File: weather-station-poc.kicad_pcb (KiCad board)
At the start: 4 copper layers, 155 x 88 mm, 135 parts, among them IC1 632723100011, IC2 TCPP01-M12, IC3 USBLC6-2SC6, IC4 BME690, IC5 S2-LPQTR, IC6 BALF-SPI2-01D3, IC7 STSAFA110S8OCD03, J1 Conn_ARM_JTAG_SWD_10, J2 61300311121, J3 61300311121, J4 61300511121, J5 61300311121, J6 687140149022, J7 687110183622, Q1 STL11N3LLH6, U1 STM32U5G9ZJTxQ, U2 BME280, U3 BMP581, Y1 NX2016SA-16MHZ-EXS00A-CS07826, Y2 NX2012SA-32.768K-STD-MUB-1, Y3 NX1612SA-50M-EXS00A-CS08403

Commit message: Update weather-station-poc.kicad_pcb
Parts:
- C1, C2, C3, C4, D1, D2, IC2, IC3, Q1, R1, R12, R13, R14, R15, R16, R17, R2, R3, R4: moved to B.Cu
- moved J5 180.7 mm to (158.0, 53.7)
- moved J3 171.5 mm to (148.9, 53.7)
- moved J2 162.4 mm to (139.7, 53.7)
- moved S2 160.4 mm to (72.0, 78.8), turned to -90 degrees
- moved J4 150.3 mm to (125.2, 53.7)
- moved R17 132.0 mm to (97.7, 72.5)
- moved C36 128.3 mm to (236.5, 94.4)
- moved C37 128.3 mm to (236.5, 96.9)
- moved C38 128.3 mm to (236.5, 99.4)
- moved C39 128.3 mm to (236.5, 101.9)
- moved C40 128.3 mm to (236.5, 104.4)
- moved C41 128.3 mm to (236.5, 107.0)
- moved R16 127.6 mm to (97.7, 75.0)
- moved U3 124.5 mm to (221.9, 86.7)
- moved IC4 124.0 mm to (222.0, 81.3)
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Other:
- board size 155 x 88 mm -> 160 x 80 mm

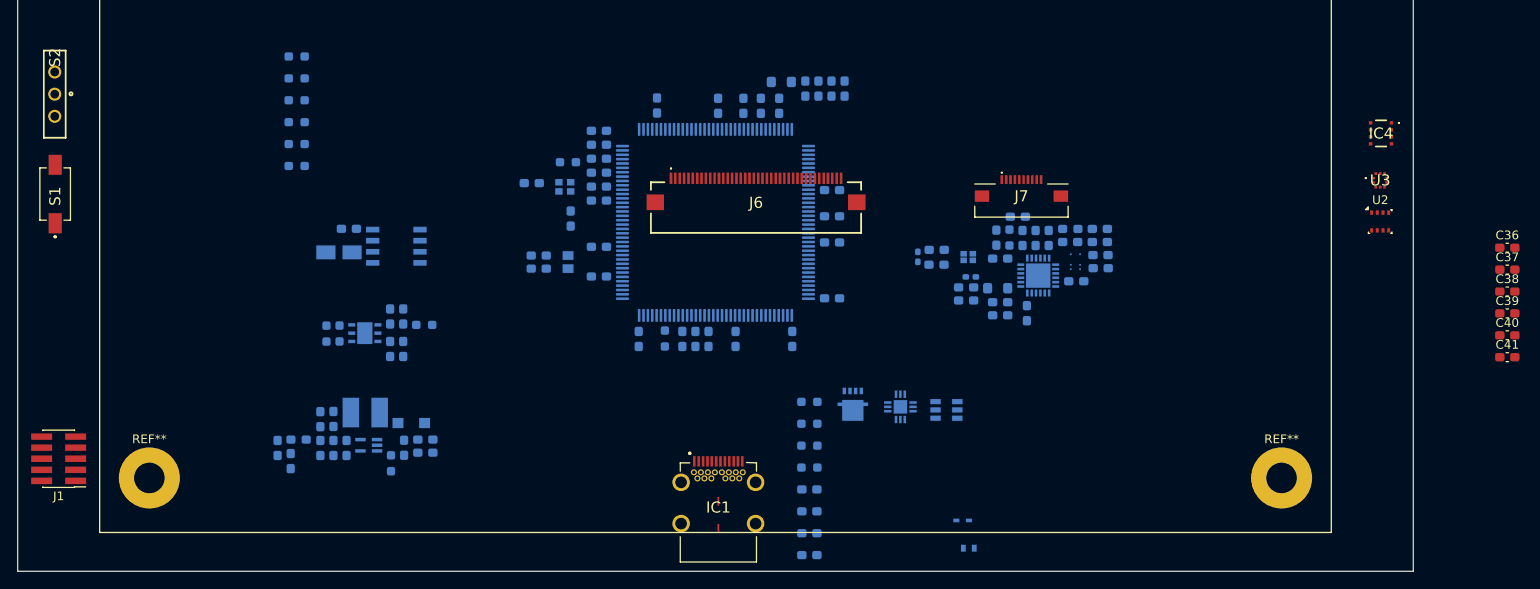
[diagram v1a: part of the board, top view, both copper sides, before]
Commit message: Place PCB top components
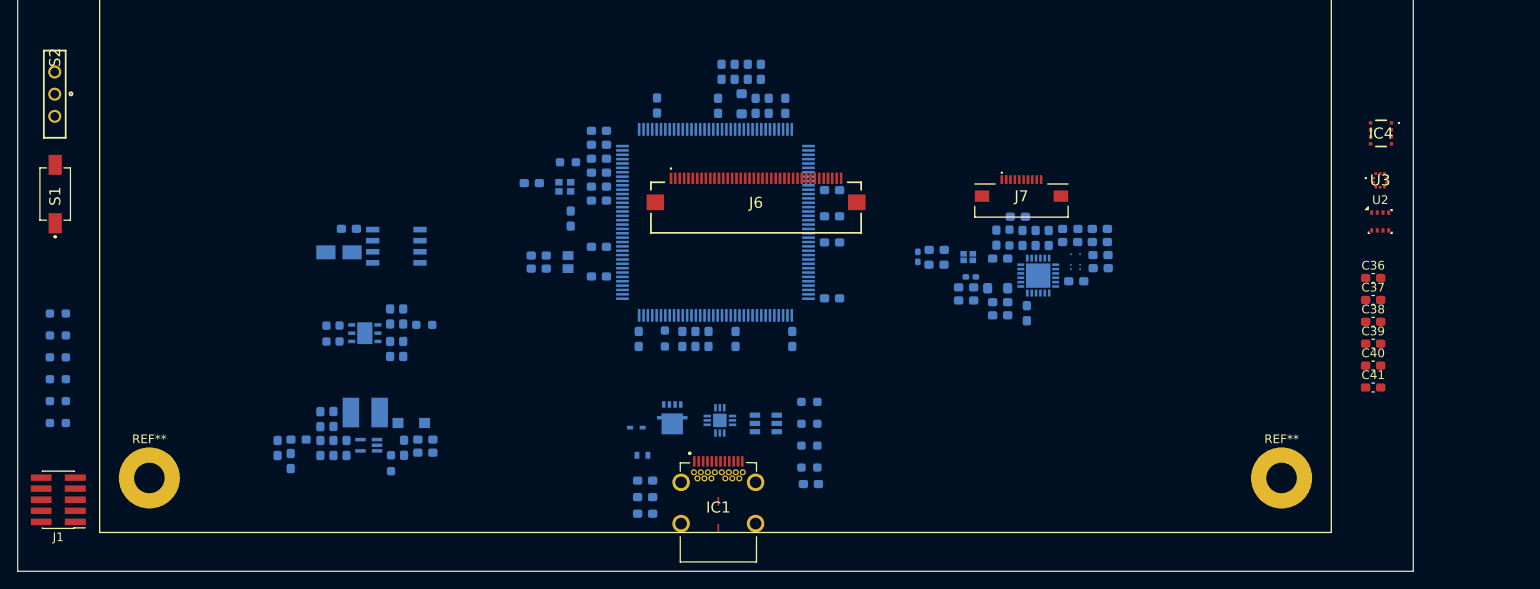
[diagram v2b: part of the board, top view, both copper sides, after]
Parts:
- moved R12 40.2 mm to (70.3, 114.5)
- moved R13 40.2 mm to (70.3, 112.0)
- moved R14 40.2 mm to (70.3, 109.5)
- moved R15 40.2 mm to (70.3, 107.0)
- moved R16 40.2 mm to (70.3, 104.5)
- moved R17 40.2 mm to (70.3, 102.0)
- moved D1 38.9 mm to (137.3, 118.2)
- moved D2 38.9 mm to (136.6, 115.0)
- moved IC2 20.8 mm to (146.2, 114.2)
- moved IC3 20.8 mm to (151.5, 114.5)
- moved Q1 20.8 mm to (140.7, 113.9)
- moved C2 19.0 mm to (137.6, 124.9)
- moved C3 18.9 mm to (137.6, 123.0)
- moved C4 18.9 mm to (137.6, 121.1)
- moved C38 15.8 mm to (221.1, 102.9)
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
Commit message: All components placed on PCB
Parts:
- moved R17 102.5 mm to (160.1, 52.5)
- moved D1 26.4 mm to (163.7, 117.5), turned to 90 degrees
- moved C2 24.9 mm to (161.4, 117.6), turned to -90 degrees
- moved C3 23.5 mm to (159.1, 113.3)
- moved Q1 22.6 mm to (163.3, 113.0), turned to -90 degrees
- moved R16 19.4 mm to (65.3, 123.2), turned to 180 degrees
- moved R15 19.4 mm to (65.3, 125.7), turned to 180 degrees
- moved R14 18.9 mm to (77.2, 127.1), turned to -90 degrees
- moved C4 17.7 mm to (155.2, 118.8), turned to -90 degrees
- moved D2 17.5 mm to (153.8, 118.3), turned to -90 degrees
- moved R13 16.1 mm to (75.7, 127.1), turned to -90 degrees
- moved R12 13.2 mm to (74.2, 127.1), turned to -90 degrees
- moved S1 10.6 mm to (68.8, 77.7), turned to 180 degrees
- moved IC2 9.03 mm to (155.2, 114.9), turned to -90 degrees
- moved S2 8.05 mm to (71.1, 70.8), turned to 0 degrees
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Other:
- board size 160 x 80 mm -> 165 x 91.2 mm

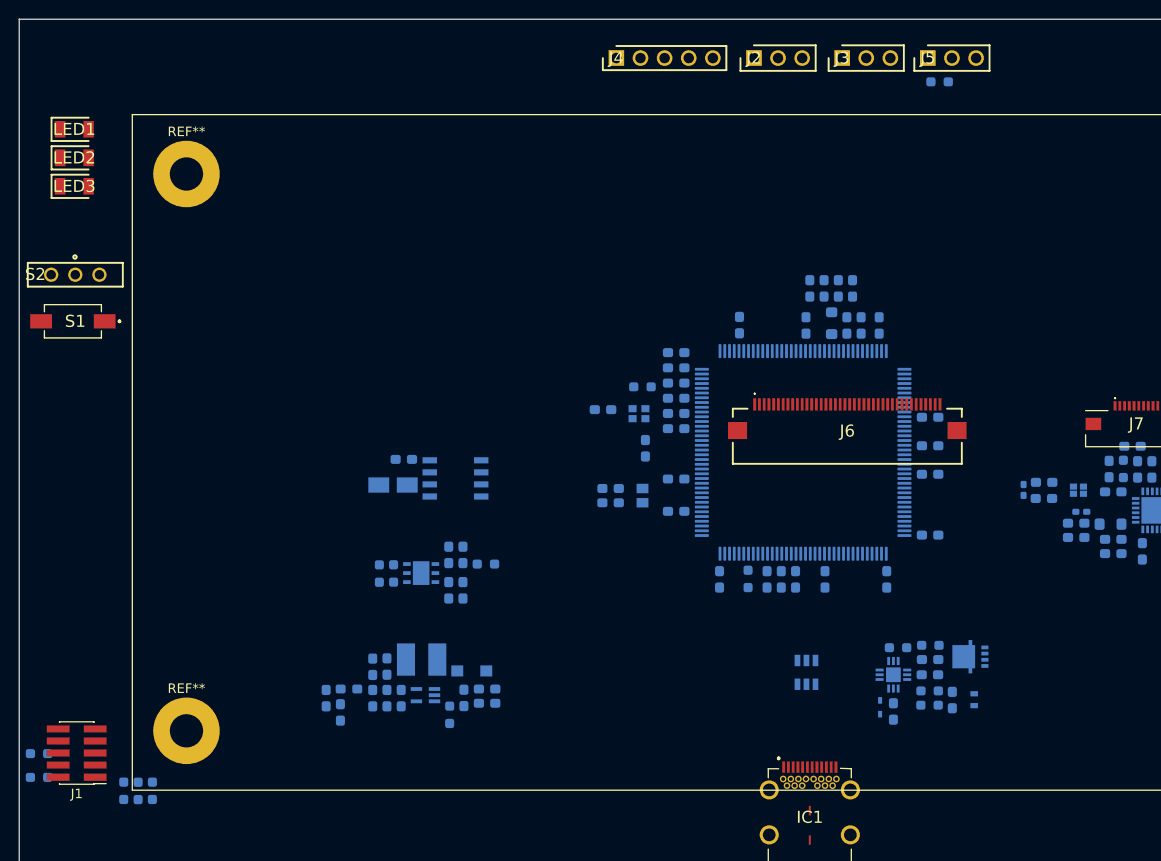
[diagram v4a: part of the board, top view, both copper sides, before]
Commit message: Add 3D models to some components and move JTAG connector
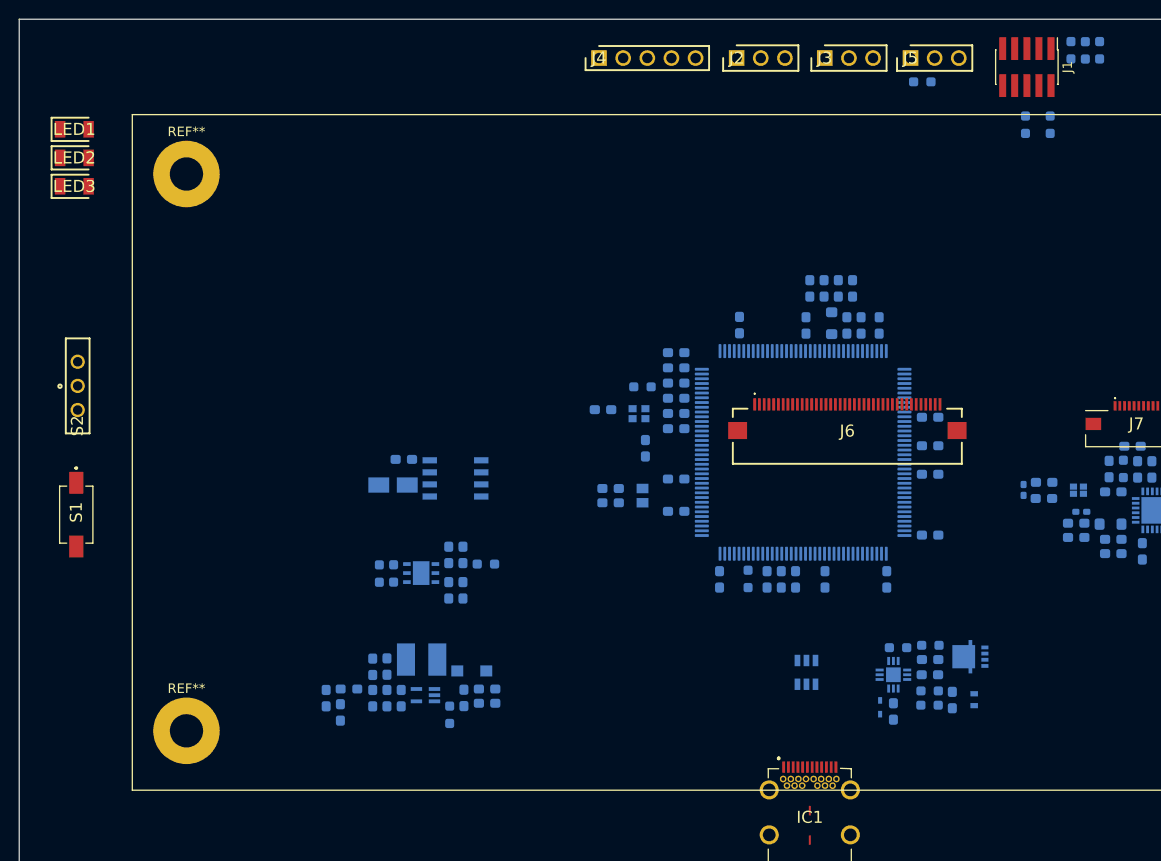
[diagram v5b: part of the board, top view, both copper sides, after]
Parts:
- moved R15 126.7 mm to (171.7, 57.0), turned to 90 degrees
- moved R13 126.5 mm to (175.4, 49.2)
- moved R14 126.5 mm to (176.9, 49.2)
- moved R12 126.5 mm to (173.9, 49.2)
- moved J1 123.3 mm to (169.2, 51.0), turned to -90 degrees
- moved R16 123.1 mm to (169.1, 57.0), turned to 90 degrees
- moved S1 20.4 mm to (69.2, 98.0), turned to -90 degrees
- moved S2 12.3 mm to (67.3, 82.5), turned to 90 degrees
- moved J2 1.82 mm to (138.7, 50.0)
- moved J3 1.82 mm to (148.0, 50.0)
- moved J4 1.82 mm to (124.2, 50.0)
- moved J5 1.82 mm to (157.0, 50.0)
- moved R17 1.82 mm to (158.2, 52.5)

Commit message: Remove L5 inductos on radio oscillator
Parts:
- renumbered L6 to L5
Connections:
- C59 pad 2: Net-(C59-Pad2) -> GND
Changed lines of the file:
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@@
 		(descr "4018")
 		(tags "Inductor")
-		(property "Reference" "L6"
+		(property "Reference" "L5"
 			(at 0 0 180)
 			(layer "B.SilkS")
@@
 			(layers "B.Cu" "B.Mask" "B.Paste")
 			(roundrect_rratio 0.25)
-			(net 23 "Net-(C59-Pad2)")
-			(pintype "passive")
-		)
+			(net 3 "GND")
+			(pintype "passive")
+		)

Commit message: Simplify S2LP schematic based on datasheet
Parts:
- renumbered C57 to C55, C55 to C56, C59 to C57, C60 to C58, C61 to C59, C62 to C60, C63 to C61, C64 to C62, C65 to C63, C66 to C64, C67 to C65, C68 to C66, C69 to C67, C70 to C68, C71 to C69, C72 to C70, C73 to C71, C74 to C72, C75 to C73, C76 to C74, L3 to L2, L4 to L3, L5 to L4
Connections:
- C55 pad 1: Net-(C57-Pad1) -> Net-(IC5-TX)
- C55 pad 2: GND -> Net-(IC6-TX)
- L2 pad 1: Net-(L2-Pad2) -> /RadioSubGHz/VSMPS2
- L3 pad 2: Net-(C57-Pad1) -> /RadioSubGHz/VSMPS2

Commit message: Place 4 others hole on the border of the PCB, TODO: place its correctly
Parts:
- added ?: , , F.Cu at (222.8, 51.2)
- added ?: , , F.Cu at (222.7, 131.5)
- added ?: , , F.Cu at (68.6, 131.3)
- added ?: , , F.Cu at (67.8, 50.6)
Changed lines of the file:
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@@
 		)
 	)
+	(footprint ""
+		(layer "F.Cu")
+		(at 222.8 51.2)
+		(property "Reference" ""
+			(at 0 0 0)
+			(layer "F.SilkS")
+			(effects
+				(font
+					(size 1.27 1.27)
+					(thickness 0.15)
+				)
+			)
+		)
+		(property "Value" ""
+			(at 0 0 0)
+			(layer "F.Fab")
+			(effects
+				(font
+					(size 1.27 1.27)
+					(thickness 0.15)
+				)
+			)
+		)
+		(property "Datasheet" ""
+			(at 0 0 0)
+			(layer "F.Fab")
+			(hide yes)
+			(effects
+				(font
+					(size 1.27 1.27)
+					(thickness 0.15)
+				)
+			)
+		)
+		(property "Description" ""
+			(at 0 0 0)
+			(layer "F.Fab")
+			(hide yes)
+			(effects
+				(font
+					(size 1.27 1.27)
+					(thickness 0.15)
+				)
+			)
+		)
+		(pad "1" thru_hole circle
+			(at 0 0)
+			(size 7 7)
+			(drill 3.5)
+			(layers "*.Cu" "*.Mask")
+			(remove_unused_layers no)
+			(zone_connect 2)
+		)
+		(embedded_fonts no)
+	)
 	(footprint "weather-station-poc-fp:LEDC3216X120N"
 		(layer "F.Cu")
@@
 		)
 	)
+	(footprint ""
+		(layer "F.Cu")
+		(at 222.7 131.5)
+		(property "Reference" ""
+			(at 0 0 0)
+			(layer "F.SilkS")
+			(effects
+				(font
+					(size 1.27 1.27)
+					(thickness 0.15)
+				)
+			)
+		)
+		(property "Value" ""
+			(at 0 0 0)
+			(layer "F.Fab")
+			(effects
+				(font
+					(size 1.27 1.27)
+					(thickness 0.15)
+				)
+			)
+		)
+		(property "Datasheet" ""
+			(at 0 0 0)
+			(layer "F.Fab")
+			(hide yes)
+			(effects
+				(font
+					(size 1.27 1.27)
+					(thickness 0.15)
+				)
+			)
+		)
+		(property "Description" ""
+			(at 0 0 0)
+			(layer "F.Fab")
+			(hide yes)
+			(effects
+				(font
+					(size 1.27 1.27)
+					(thickness 0.15)
+				)
+			)
+		)
+		(pad "1" thru_hole circle
+			(at 0 0)
+			(size 7 7)
+			(drill 3.5)
+			(layers "*.Cu" "*.Mask")
+			(remove_unused_layers no)
+			(zone_connect 2)
+		)
+		(embedded_fonts no)
+	)
+	(footprint ""
+		(layer "F.Cu")
+		(at 68.6 131.3)
+		(property "Reference" ""
+			(at 0 0 0)
+			(layer "F.SilkS")
+			(effects
+				(font
+					(size 1.27 1.27)
+					(thickness 0.15)
+				)
+			)
+		)
+		(property "Value" ""
+			(at 0 0 0)
+			(layer "F.Fab")
+			(effects
+				(font
+					(size 1.27 1.27)
+					(thickness 0.15)
+				)
+			)
+		)
+		(property "Datasheet" ""
+			(at 0 0 0)
+			(layer "F.Fab")
+			(hide yes)
+			(effects
+				(font
+					(size 1.27 1.27)
+					(thickness 0.15)
+				)
+			)
+		)
+		(property "Description" ""
+			(at 0 0 0)
+			(layer "F.Fab")
+			(hide yes)
+			(effects
+				(font
+					(size 1.27 1.27)
+					(thickness 0.15)
+				)
+			)
+		)
+		(pad "1" thru_hole circle
+			(at 0 0)
+			(size 7 7)
+			(drill 3.5)
+			(layers "*.Cu" "*.Mask")
+			(remove_unused_layers no)
+			(zone_connect 2)
+		)
+		(embedded_fonts no)
+	)
 	(footprint "Connector_PinHeader_1.27mm:PinHeader_2x05_P1.27mm_Vertical_SMD"
 		(layer "F.Cu")
@@
 		)
 	)
+	(footprint ""
+		(layer "F.Cu")
+		(at 67.8 50.6)
+		(property "Reference" ""
+			(at 0 0 0)
+			(layer "F.SilkS")
+			(effects
+				(font
+					(size 1.27 1.27)
+					(thickness 0.15)
+				)
+			)
+		)
+		(property "Value" ""
+			(at 0 0 0)
+			(layer "F.Fab")
+			(effects
+				(font
+					(size 1.27 1.27)
+					(thickness 0.15)
+				)
+			)
+		)
+		(property "Datasheet" ""
+			(at 0 0 0)
+			(layer "F.Fab")
+			(hide yes)
+			(effects
+				(font
+					(size 1.27 1.27)
+					(thickness 0.15)
+				)
+			)
+		)
+		(property "Description" ""
+			(at 0 0 0)
+			(layer "F.Fab")
+			(hide yes)
+			(effects
+				(font
+					(size 1.27 1.27)
+					(thickness 0.15)
+				)
+			)
+		)
+		(pad "1" thru_hole circle
+			(at 0 0)
+			(size 7 7)
+			(drill 3.5)
+			(layers "*.Cu" "*.Mask")
+			(remove_unused_layers no)
+			(zone_connect 2)
+		)
+		(embedded_fonts no)
+	)
 	(footprint "weather-station-poc-fp:HDRV3W64P0X254_1X3_762X254X869P"
